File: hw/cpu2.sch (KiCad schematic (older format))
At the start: 0 parts

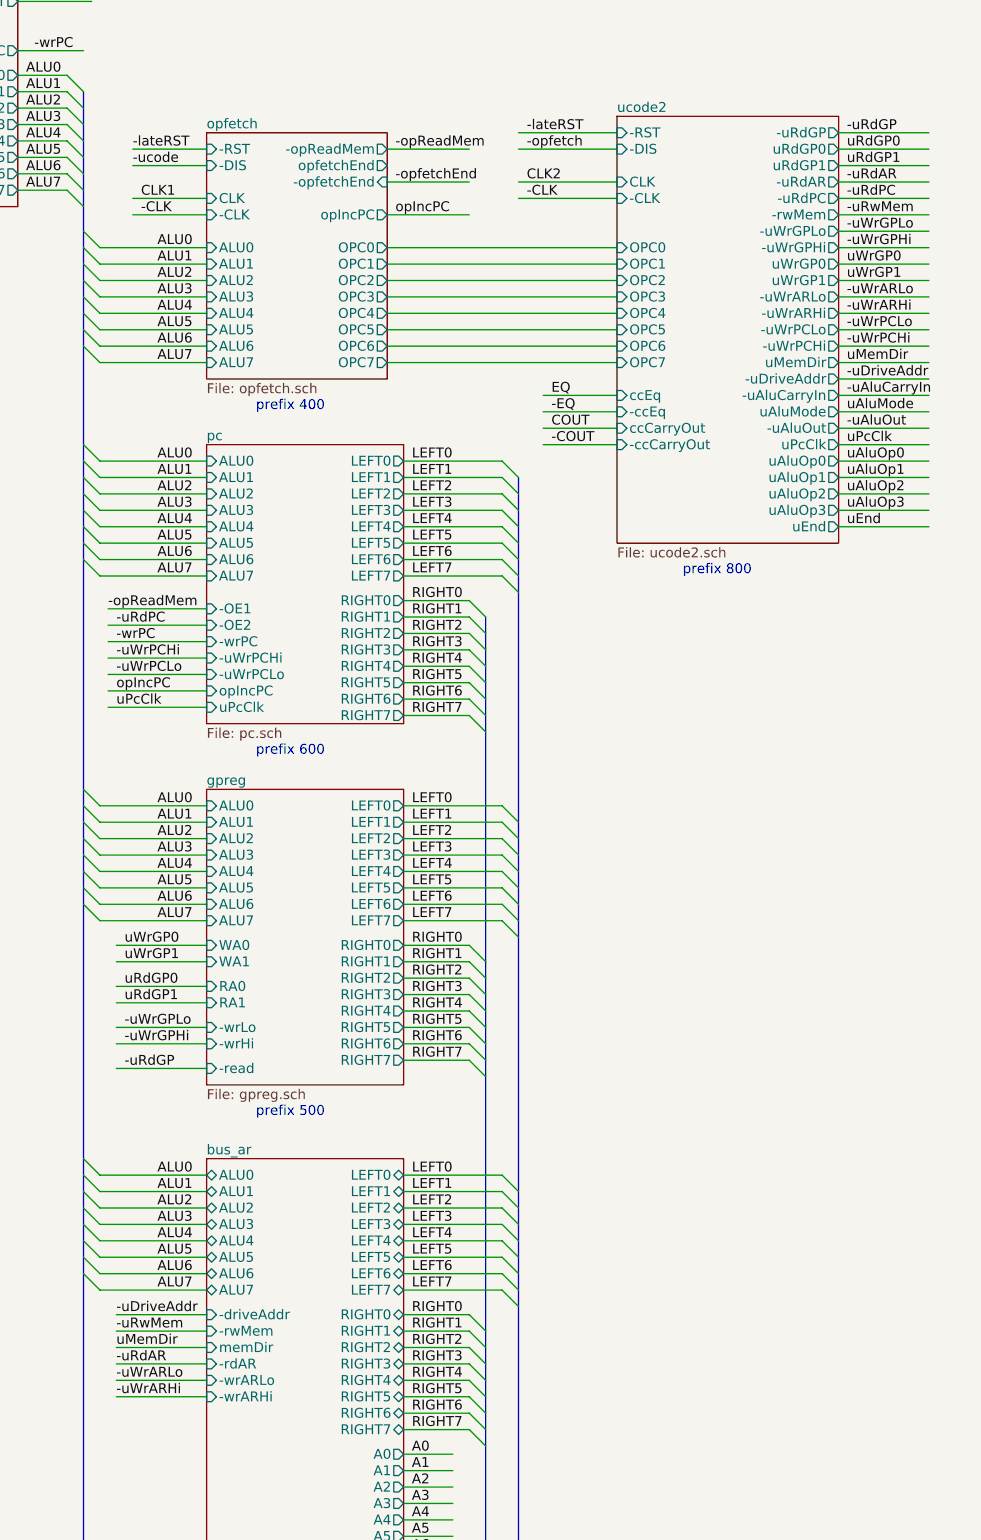
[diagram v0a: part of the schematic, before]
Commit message: use '573 latches as address bus drivers
This let's us latch the address being asserted onto
the left/right ALU inputs busses in case it is going
to change during the execution of the instruction.
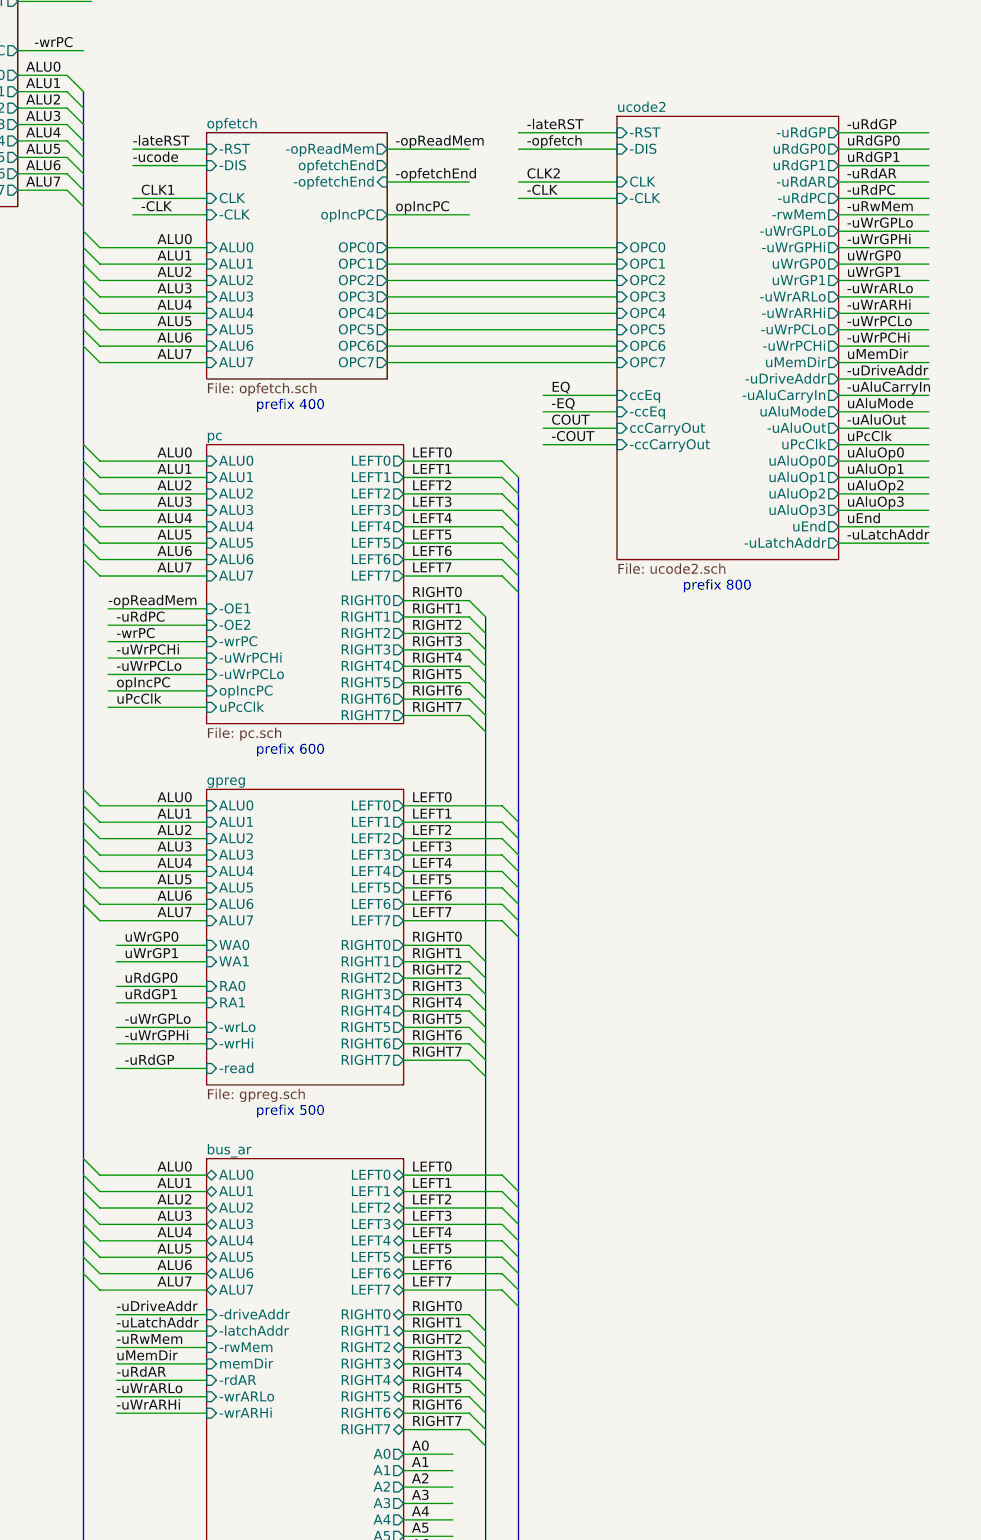
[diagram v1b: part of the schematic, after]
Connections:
- net labels added: -uLatchAddr
- wire segments 231 -> 233
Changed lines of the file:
@@
 Text Notes 6150 3400 0    60   ~ 0
 prefix 400
-Text Notes 8750 4400 0    60   ~ 0
+Text Notes 8750 4500 0    60   ~ 0
 prefix 800
 Text Notes 6150 5500 0    60   ~ 0
@@
 	10000 13050 10100 13150
 $Sheet
-S 8350 1600 1350 2600
+S 8350 1600 1350 2700
 U 594ECB9B
 F0 "ucode2" 60
@@
 F41 "-rwMem" O R 9700 2200 60
 F42 "uMemDir" O R 9700 3100 60
+F43 "-uLatchAddr" O R 9700 4200 60
 $EndSheet
 Wire Wire Line
@@
 F25 "RIGHT7" B R 7050 9600 60
 F26 "-driveAddr" I L 5850 8900 60
-F27 "-rwMem" I L 5850 9000 60
-F28 "memDir" I L 5850 9100 60
-F29 "-rdAR" I L 5850 9200 60
-F30 "-wrARLo" I L 5850 9300 60
-F31 "-wrARHi" I L 5850 9400 60
+F27 "-rwMem" I L 5850 9100 60
+F28 "memDir" I L 5850 9200 60
+F29 "-rdAR" I L 5850 9300 60
+F30 "-wrARLo" I L 5850 9400 60
+F31 "-wrARHi" I L 5850 9500 60
 F32 "A0" O R 7050 9750 60
 F33 "A1" O R 7050 9850 60
@@
 F54 "D6" B R 7050 12000 60
 F55 "D7" B R 7050 12100 60
+F56 "-latchAddr" I L 5850 9000 60
 $EndSheet
 Wire Wire Line
@@
 	5850 8900 5300 8900
 Wire Wire Line
-	5850 9000 5300 9000
-Wire Wire Line
 	5850 9100 5300 9100
 Wire Wire Line
@@
 Wire Wire Line
 	5850 9400 5300 9400
+Wire Wire Line
+	5850 9500 5300 9500
 Text Label 5300 8900 0    60   ~ 0
 -uDriveAddr
-Text Label 5300 9000 0    60   ~ 0
+Text Label 5300 9100 0    60   ~ 0
 -uRwMem
-Text Label 5300 9100 0    60   ~ 0
+Text Label 5300 9200 0    60   ~ 0
 uMemDir
-Text Label 5300 9200 0    60   ~ 0
+Text Label 5300 9300 0    60   ~ 0
 -uRdAR
-Text Label 5300 9300 0    60   ~ 0
+Text Label 5300 9400 0    60   ~ 0
 -uWrARLo
-Text Label 5300 9400 0    60   ~ 0
+Text Label 5300 9500 0    60   ~ 0
 -uWrARHi
 Wire Wire Line
@@
 Text Label 7800 1700 0    60   ~ 0
 -lateRST
+Wire Wire Line
+	5850 9000 5300 9000
+Text Label 5300 9000 0    60   ~ 0
+-uLatchAddr
+Wire Wire Line
+	9700 4200 10250 4200
+Text Label 9750 4200 0    60   ~ 0
+-uLatchAddr
 $EndSCHEMATC

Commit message: add -uExtW/-uExtR signals to main schematic
Also, don't need to export the -uExtRW signal via a
hierarchical pin.
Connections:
- net labels added: -uExtR, -uExtW
- wire segments 233 -> 235
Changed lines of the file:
@@
 Text Notes 6150 3400 0    60   ~ 0
 prefix 400
-Text Notes 8750 4500 0    60   ~ 0
+Text Notes 8750 4700 0    60   ~ 0
 prefix 800
 Text Notes 6150 5500 0    60   ~ 0
@@
 	10000 13050 10100 13150
 $Sheet
-S 8350 1600 1350 2700
+S 8350 1600 1350 2900
 U 594ECB9B
 F0 "ucode2" 60
@@
 F42 "uMemDir" O R 9700 3100 60
 F43 "-uLatchAddr" O R 9700 4200 60
+F44 "-uExtW" O R 9700 4300 60
+F45 "-uExtR" O R 9700 4400 60
 $EndSheet
 Wire Wire Line
@@
 Text Label 9750 4200 0    60   ~ 0
 -uLatchAddr
+Wire Wire Line
+	9700 4300 10250 4300
+Wire Wire Line
+	9700 4400 10250 4400
+Text Label 9750 4300 0    60   ~ 0
+-uExtW
+Text Label 9750 4400 0    60   ~ 0
+-uExtR
 $EndSCHEMATC

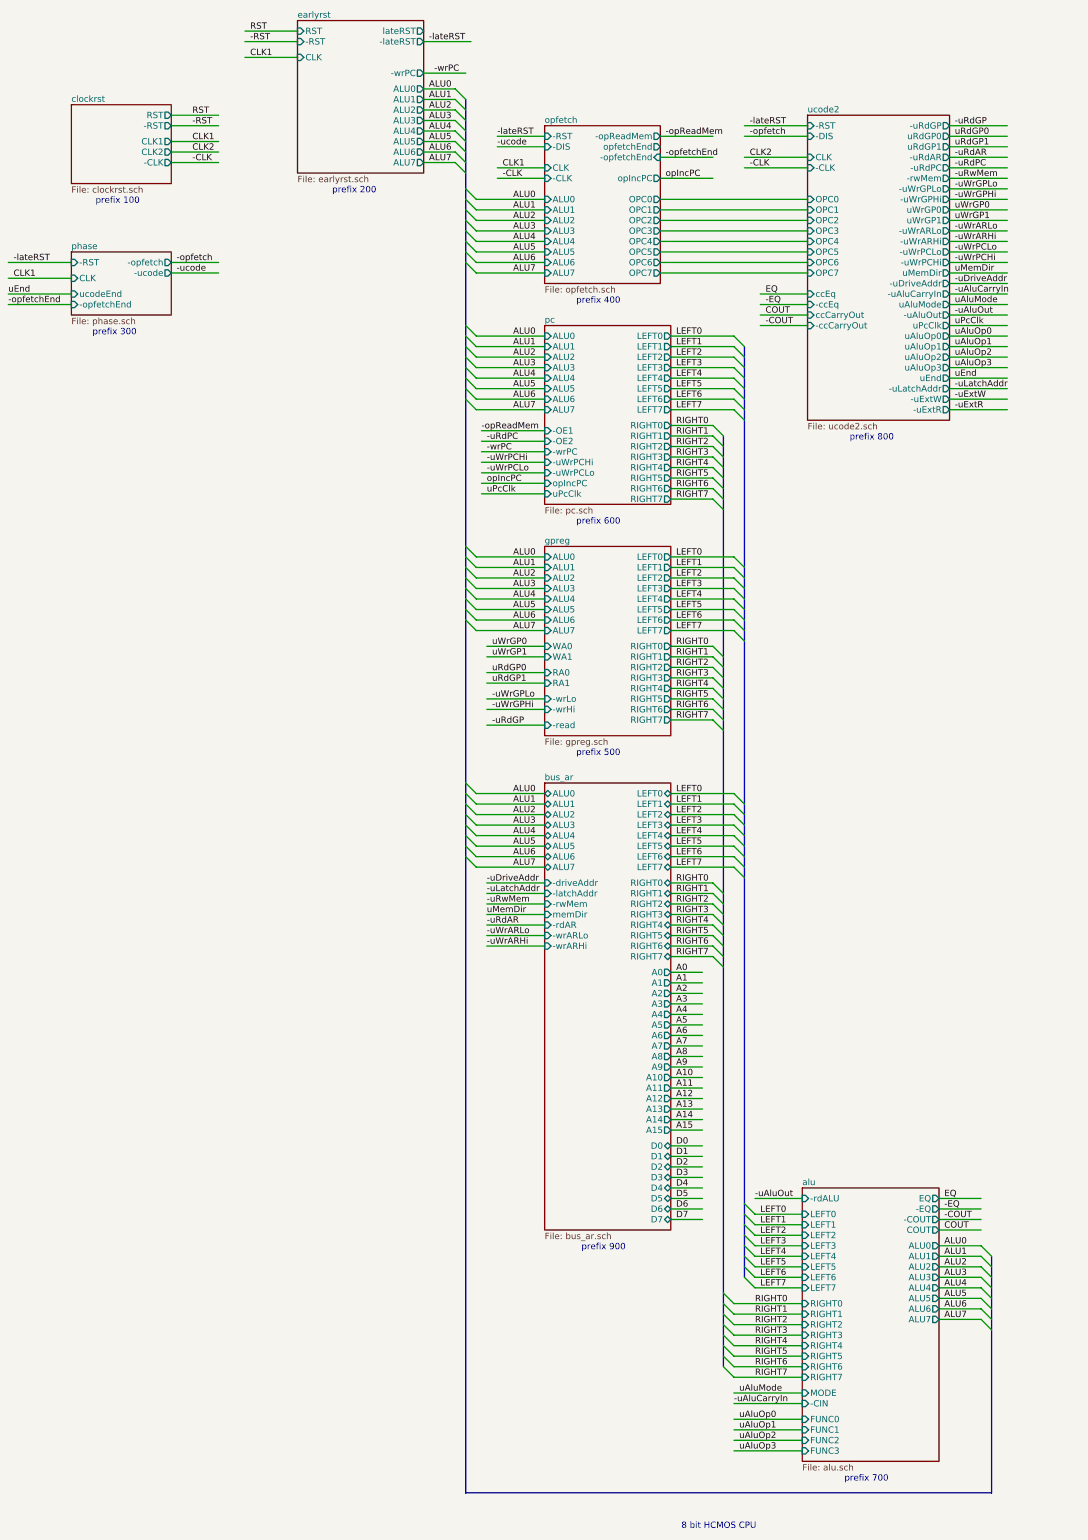
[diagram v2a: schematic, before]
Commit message: add explicit signal to latch condition codes
Was able to use microcode bits more efficiently (to make
room for the new signal) by putting the combinational
logic to generate the external read/write signals after
the '175 microcode signal registers.  This should be fine
as long as memDir is set appropriately before the extRW
signal is asserted.  (No glitches should be possible.)
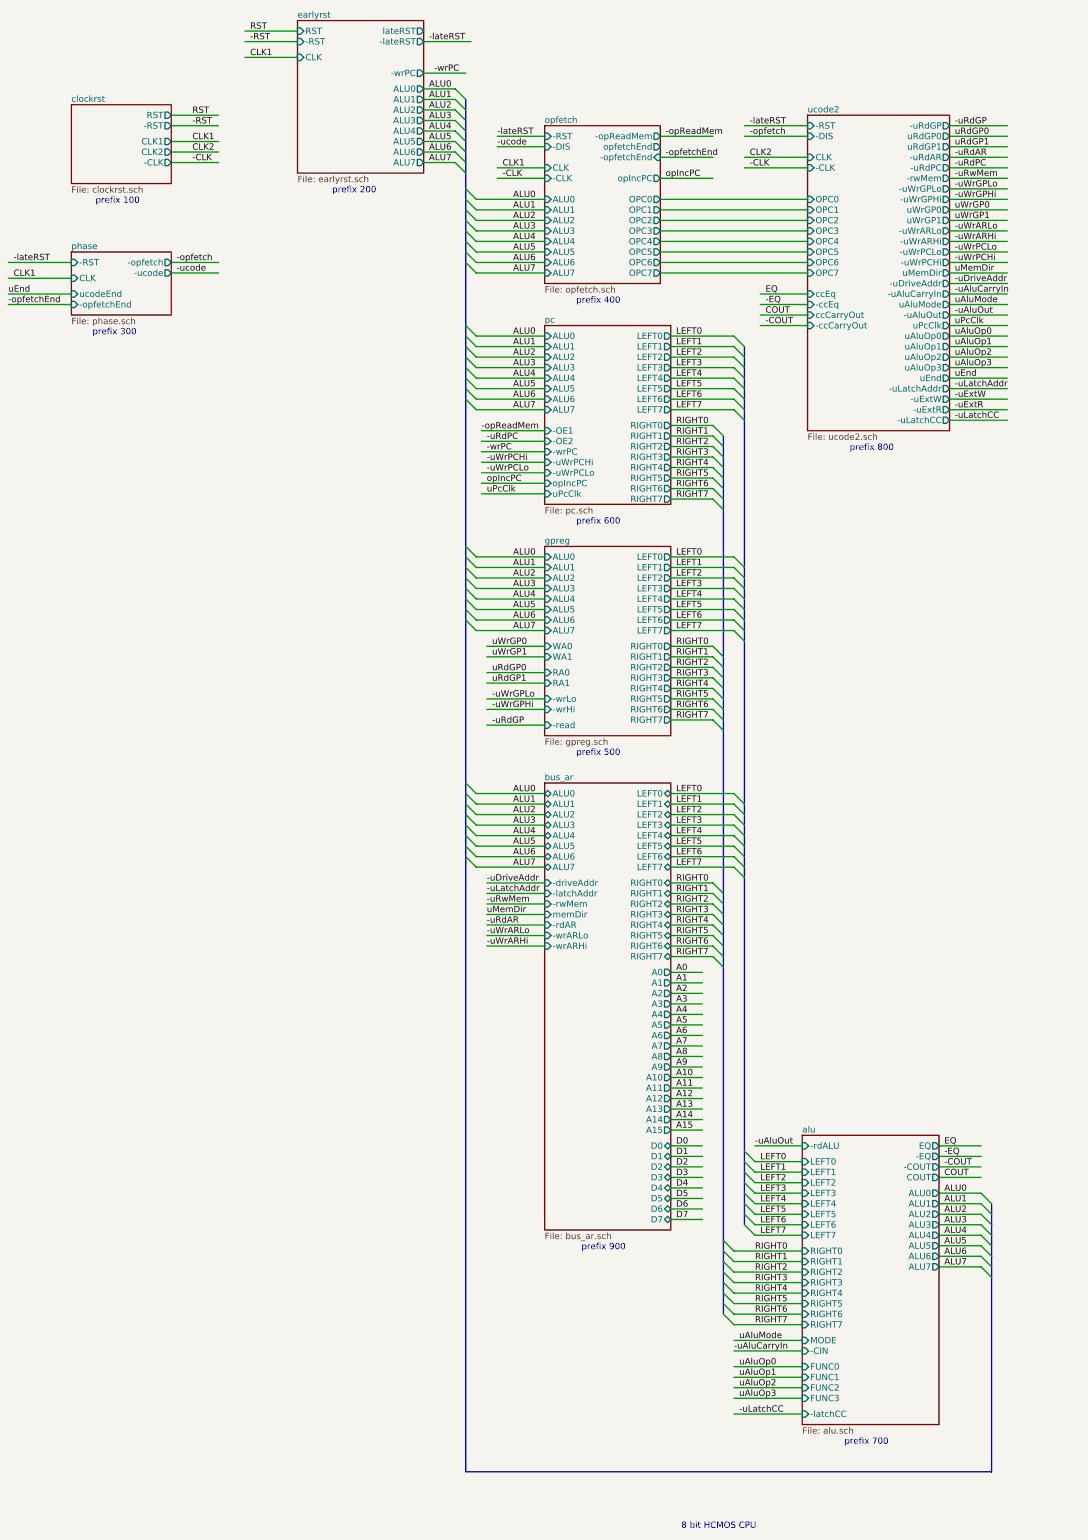
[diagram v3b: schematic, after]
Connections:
- net labels added: -uLatchCC
- wire segments 235 -> 237

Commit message: remove AR registers, switch to new ucode impl
Note that there is a bug in the ucode module:
the -uExtW and -uExtR signals are generated incorrectly.
(They need to be OR gates, not AND gates, so that
they can be held high when -uExtRW is not asserted.)
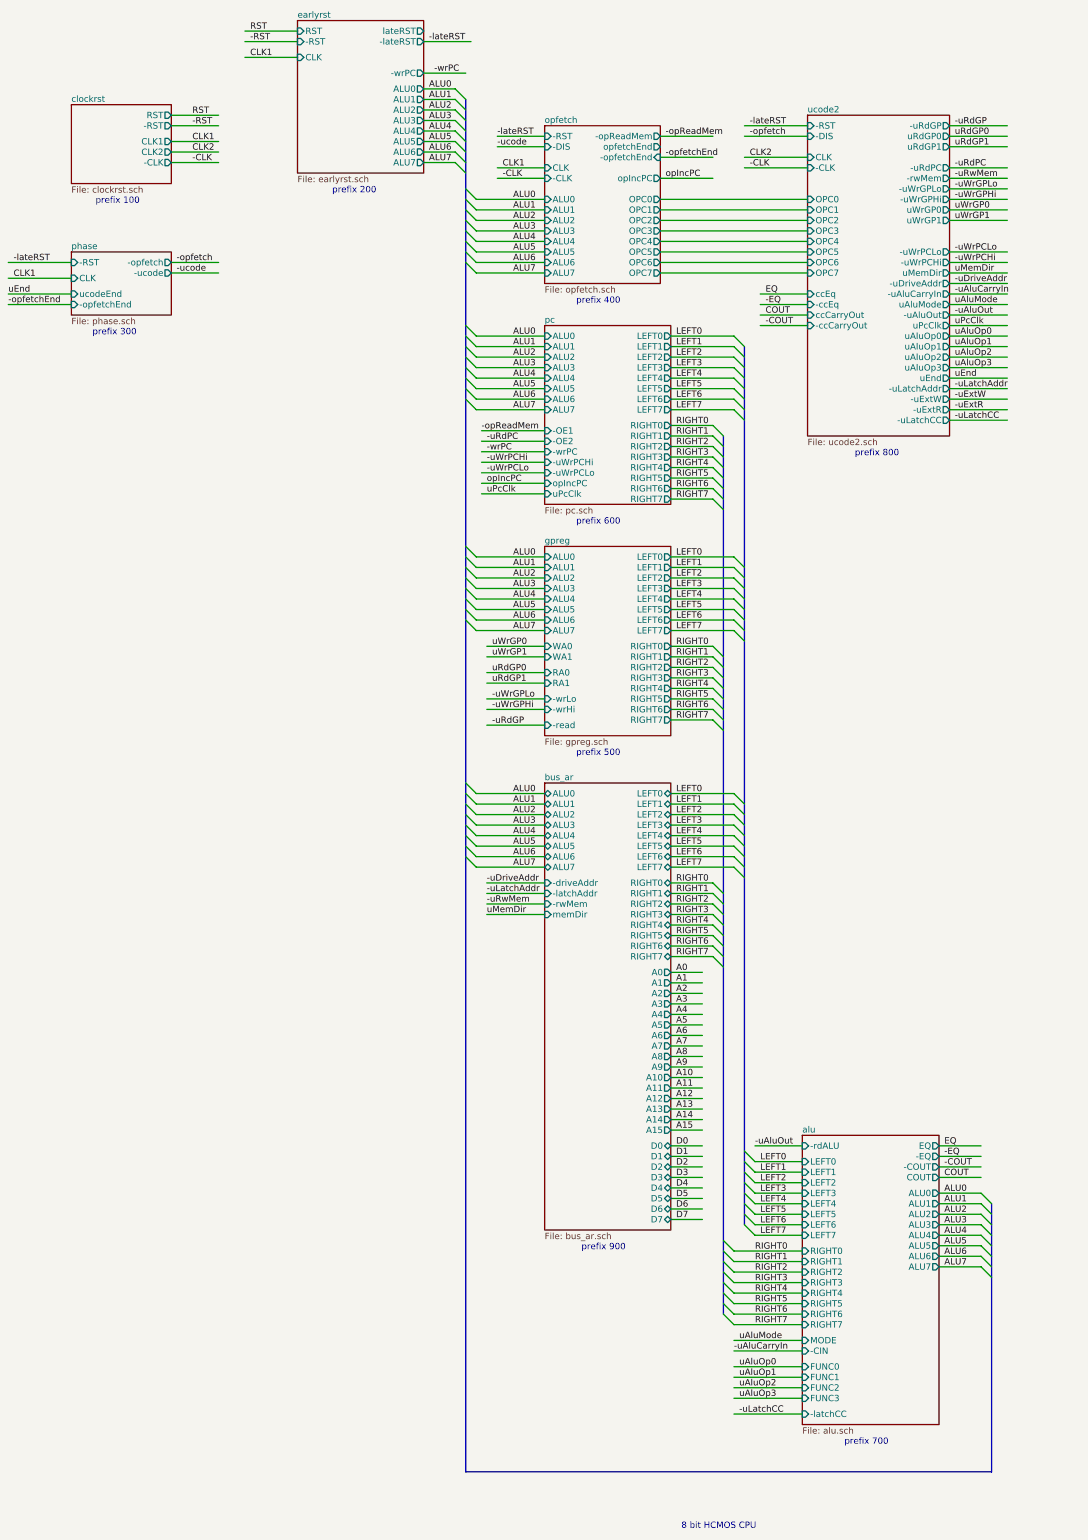
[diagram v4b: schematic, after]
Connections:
- net labels removed: -uRdAR, -uWrARHi, -uWrARLo
- wire segments 237 -> 231
